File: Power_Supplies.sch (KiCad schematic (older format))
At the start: 82 parts, among them J1 Conn_HDR_2x10_latching, M1 2N7002BK, M2 2N7002BK, Q11 2N7002BK, Q12 2N7002BK, Q13 2N7002BK, Q14 2N7002BK, Q6 2N7002BK, Q7 2N7002BK, Q8 2N7002BK, Q9 2N7002BK, U22 BD50FC0WEFJ-E2, U23 LDL212D33R

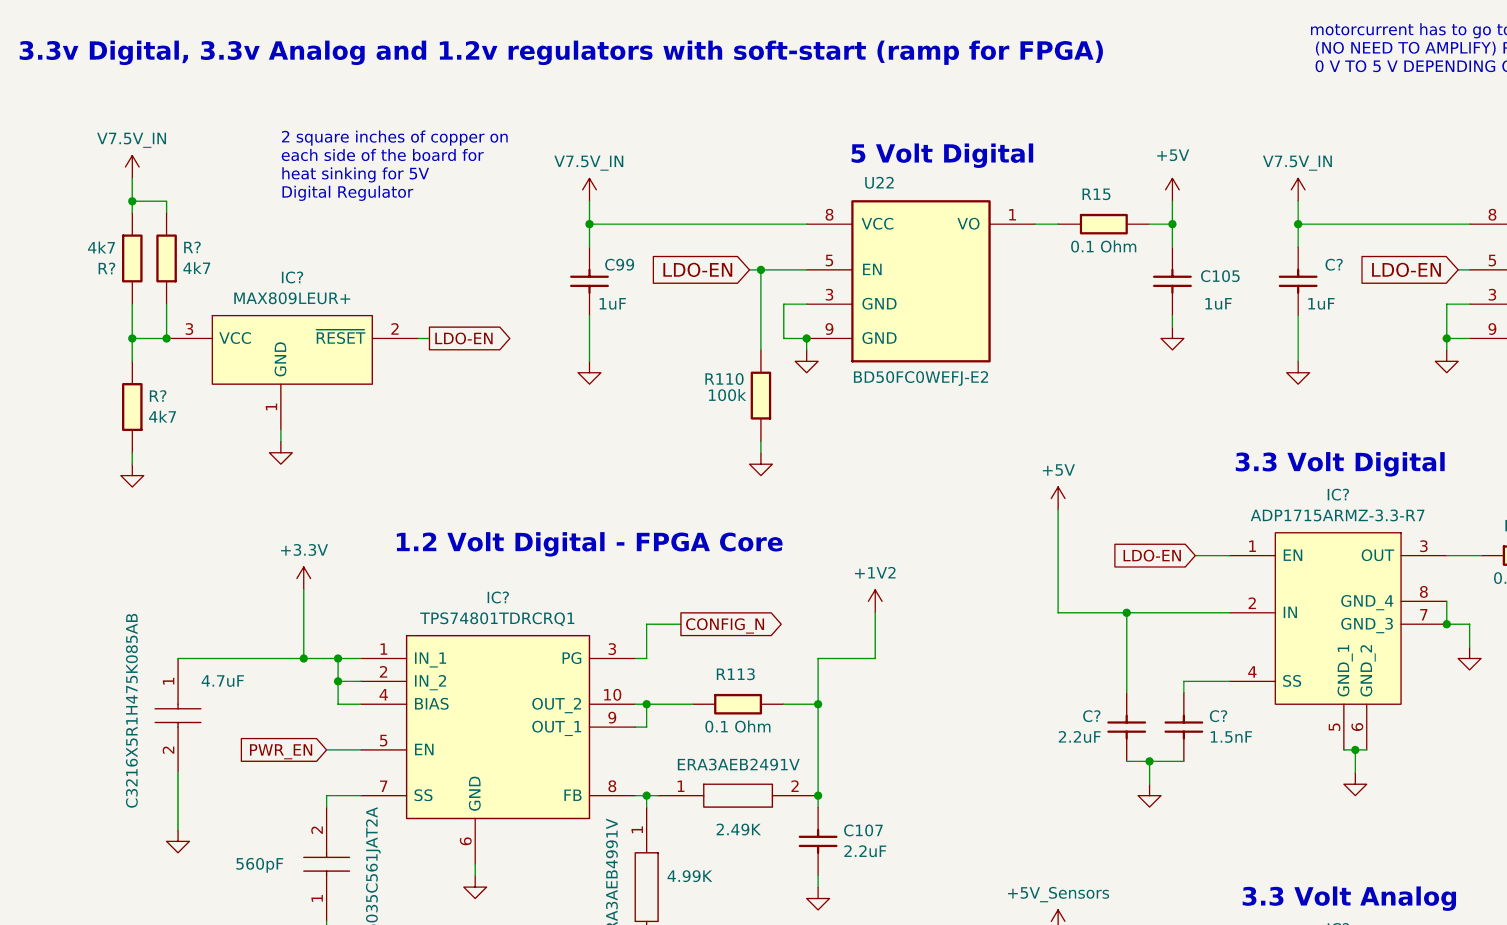
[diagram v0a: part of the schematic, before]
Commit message: Update Power_Supplies.sch
changed 7.5v_in for regulators to v7.5 after filter..
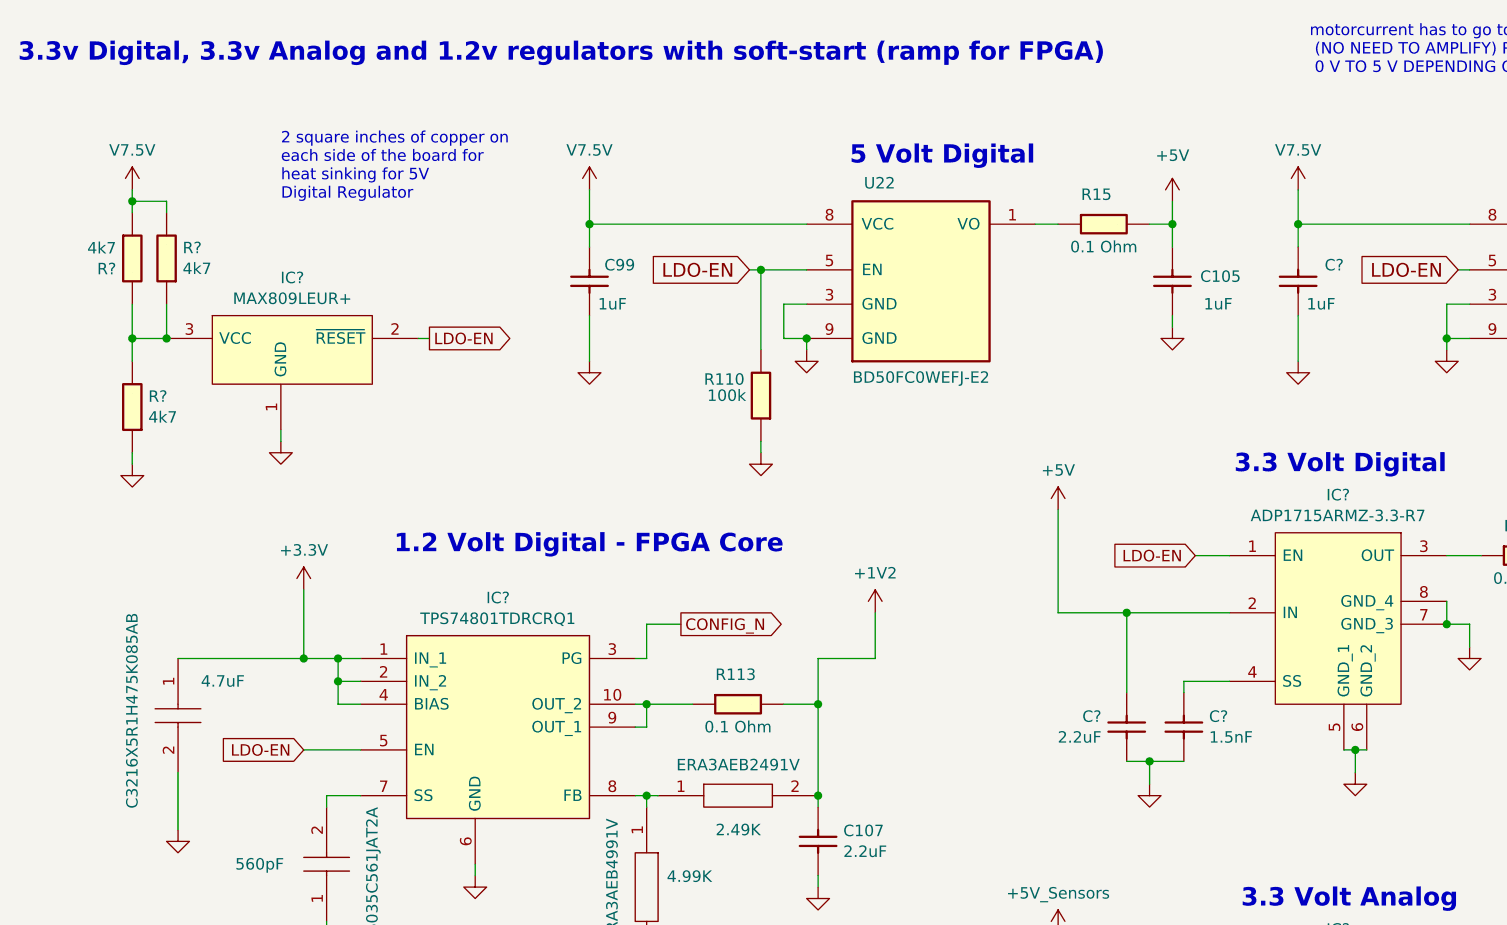
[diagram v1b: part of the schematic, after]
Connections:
- net PWR_EN is gone; now on net LDO-EN: IC?.5 (EN)
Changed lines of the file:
@@
 	1    0    0    -1
 $EndComp
-Text GLabel 1550 3250 0    50   Input ~ 0
-PWR_EN
 Wire Wire Line
 	3550 3050 3700 3050
@@
 	4850 7200 5000 7200
 Connection ~ 5300 6450
-$Comp
-L OpenVent:V7.5V_IN #PWR0162
-U 1 1 60A27BFC
-P 700 750
-F 0 "#PWR0162" H 700 600 50  0001 C CNN
-F 1 "V7.5V_IN" H 700 923 50  0000 C CNN
-F 2 "" H 700 750 50  0001 C CNN
-F 3 "" H 700 750 50  0001 C CNN
-	1    700  750
-	1    0    0    -1
-$EndComp
 Wire Wire Line
 	850  4550 850  4600
@@
 Wire Wire Line
 	700  850  850  850
-Wire Wire Line
-	700  750  700  850
-Connection ~ 700  850
 Wire Wire Line
 	6550 1450 6450 1450
@@
 	6450 1500 6450 1450
 Connection ~ 6450 1450
-Connection ~ 5800 950
 $Comp
 L OpenVent:+5V_Sensors #PWR?
@@
 	3650 1500 3650 1450
 Connection ~ 3650 1450
-$Comp
-L OpenVent:V7.5V_IN #PWR?
-U 1 1 60E0217D
-P 5800 850
-F 0 "#PWR?" H 5800 700 50  0001 C CNN
-F 1 "V7.5V_IN" H 5800 1023 50  0000 C CNN
-F 2 "" H 5800 850 50  0001 C CNN
-F 3 "" H 5800 850 50  0001 C CNN
-	1    5800 850
-	1    0    0    -1
-$EndComp
-Wire Wire Line
-	5800 850  5800 950
-$Comp
-L OpenVent:V7.5V_IN #PWR?
-U 1 1 60E1DD65
-P 2700 850
-F 0 "#PWR?" H 2700 700 50  0001 C CNN
-F 1 "V7.5V_IN" H 2700 1023 50  0000 C CNN
-F 2 "" H 2700 850 50  0001 C CNN
-F 3 "" H 2700 850 50  0001 C CNN
-	1    2700 850
-	1    0    0    -1
-$EndComp
-Wire Wire Line
-	2700 850  2700 950
-Connection ~ 2700 950
 $Comp
 L OpenVent:+3.3V #PWR?
@@
 Connection ~ 8000 950
 Wire Wire Line
-	1700 3250 1550 3250
-Wire Wire Line
 	4750 4050 4750 4550
 Wire Wire Line
@@
 	1    0    0    -1
 $EndComp
+Text GLabel 1450 3250 0    50   Input ~ 0
+LDO-EN
+Wire Wire Line
+	1450 3250 1700 3250
+$Comp
+L OpenVent:V7.5V #PWR?
+U 1 1 60A299E8
+P 5800 800
+F 0 "#PWR?" H 5800 650 50  0001 C CNN
+F 1 "V7.5V" H 5800 973 50  0000 C CNN
+F 2 "" H 5800 800 50  0001 C CNN
+F 3 "" H 5800 800 50  0001 C CNN
+	1    5800 800
+	1    0    0    -1
+$EndComp
+$Comp
+L OpenVent:V7.5V #PWR?
+U 1 1 60A29F0E
+P 2700 800
+F 0 "#PWR?" H 2700 650 50  0001 C CNN
+F 1 "V7.5V" H 2700 973 50  0000 C CNN
+F 2 "" H 2700 800 50  0001 C CNN
+F 3 "" H 2700 800 50  0001 C CNN
+	1    2700 800
+	1    0    0    -1
+$EndComp
+Wire Wire Line
+	5800 800  5800 950
+Connection ~ 5800 950
+Wire Wire Line
+	2700 800  2700 950
+Connection ~ 2700 950
+$Comp
+L OpenVent:V7.5V #PWR?
+U 1 1 60A947BC
+P 700 800
+F 0 "#PWR?" H 700 650 50  0001 C CNN
+F 1 "V7.5V" H 700 973 50  0000 C CNN
+F 2 "" H 700 800 50  0001 C CNN
+F 3 "" H 700 800 50  0001 C CNN
+	1    700  800
+	1    0    0    -1
+$EndComp
+Wire Wire Line
+	700  800  700  850
+Connection ~ 700  850
 $EndSCHEMATC

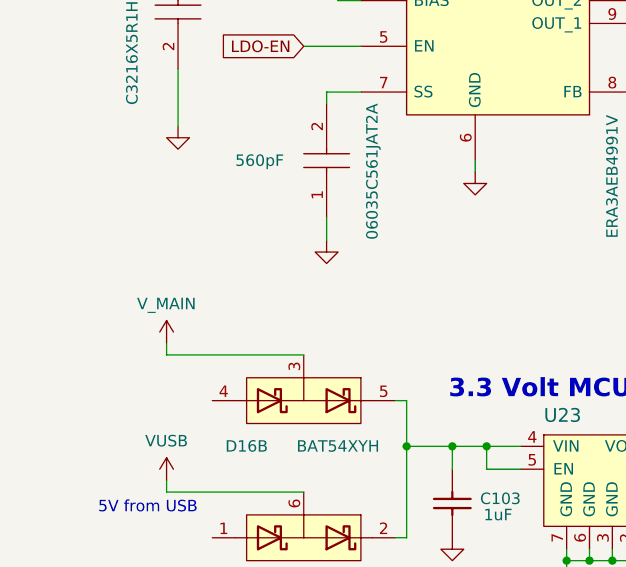
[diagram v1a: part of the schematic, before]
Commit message: Update Power_Supplies.sch
7.5V input signals corrected for regulator
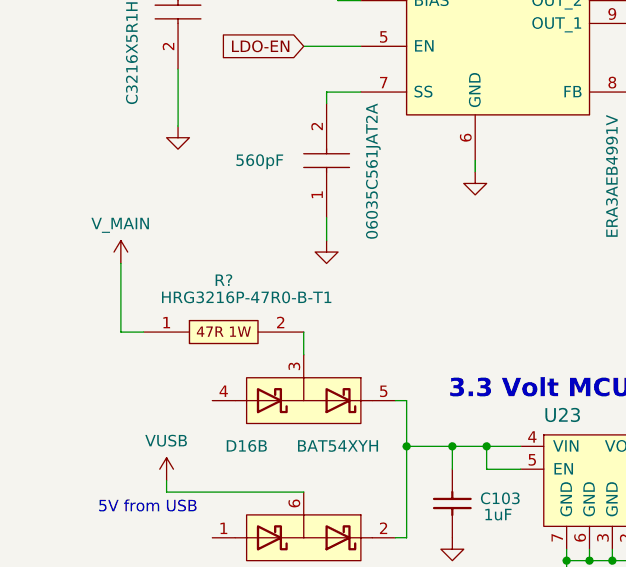
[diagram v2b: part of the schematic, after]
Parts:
- added R?: HRG3216P-47R0-B-T1, RESC3216X55N, symbol OpenVent:HRG3216P-47R0-B-T1
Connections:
- net V_MAIN: now also R?.1; no longer D16.3 (A3;K4)
- new net: D16.3 (A3;K4), R?.2
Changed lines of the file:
@@
 	850  5200 1450 5200
-Wire Wire Line
-	1450 4600 850  4600
 Wire Wire Line
 	2950 6700 2950 6550
@@
 	4850 7200 5000 7200
 Connection ~ 5300 6450
-Wire Wire Line
-	850  4550 850  4600
 Text Notes 6400 6700 2    50   ~ 0
 Power UP LED
@@
 L OpenVent:V_MAIN #PWR0160
 U 1 1 60C8A7AC
-P 850 4550
-F 0 "#PWR0160" H 850 4400 50  0001 C CNN
-F 1 "V_MAIN" H 850 4723 50  0000 C CNN
-F 2 "" H 850 4550 50  0001 C CNN
-F 3 "" H 850 4550 50  0001 C CNN
-	1    850  4550
+P 650 4200
+F 0 "#PWR0160" H 650 4050 50  0001 C CNN
+F 1 "V_MAIN" H 650 4373 50  0000 C CNN
+F 2 "" H 650 4200 50  0001 C CNN
+F 3 "" H 650 4200 50  0001 C CNN
+	1    650  4200
 	1    0    0    -1
 $EndComp
@@
 	700  800  700  850
 Connection ~ 700  850
+$Comp
+L OpenVent:HRG3216P-47R0-B-T1 R?
+U 1 1 60A949A4
+P 750 4500
+F 0 "R?" H 1100 4725 50  0000 C CNN
+F 1 "HRG3216P-47R0-B-T1" H 1200 4650 50  0000 C CNN
+F 2 "RESC3216X55N" H 1300 4550 50  0001 L CNN
+F 3 "http://www.susumu.co.jp/common/pdf/n_catalog_partition24_en.pdf" H 1300 4450 50  0001 L CNN
+F 4 "RES SMD 47 OHM 0.1% 1W 1206" H 1300 4350 50  0001 L CNN "Description"
+F 5 "0.55" H 1300 4250 50  0001 L CNN "Height"
+F 6 "Susumu" H 1300 4150 50  0001 L CNN "Manufacturer_Name"
+F 7 "HRG3216P-47R0-B-T1" H 1300 4050 50  0001 L CNN "Manufacturer_Part_Number"
+F 8 "754-HRG3216P47R0BT1" H 1300 3950 50  0001 L CNN "Mouser Part Number"
+F 9 "https://www.mouser.com/Search/Refine.aspx?Keyword=754-HRG3216P47R0BT1" H 1300 3850 50  0001 L CNN "Mouser Price/Stock"
+	1    750  4500
+	1    0    0    -1
+$EndComp
+Wire Wire Line
+	1450 4500 1450 4600
+Wire Wire Line
+	750  4500 650  4500
+Wire Wire Line
+	650  4200 650  4500
 $EndSCHEMATC

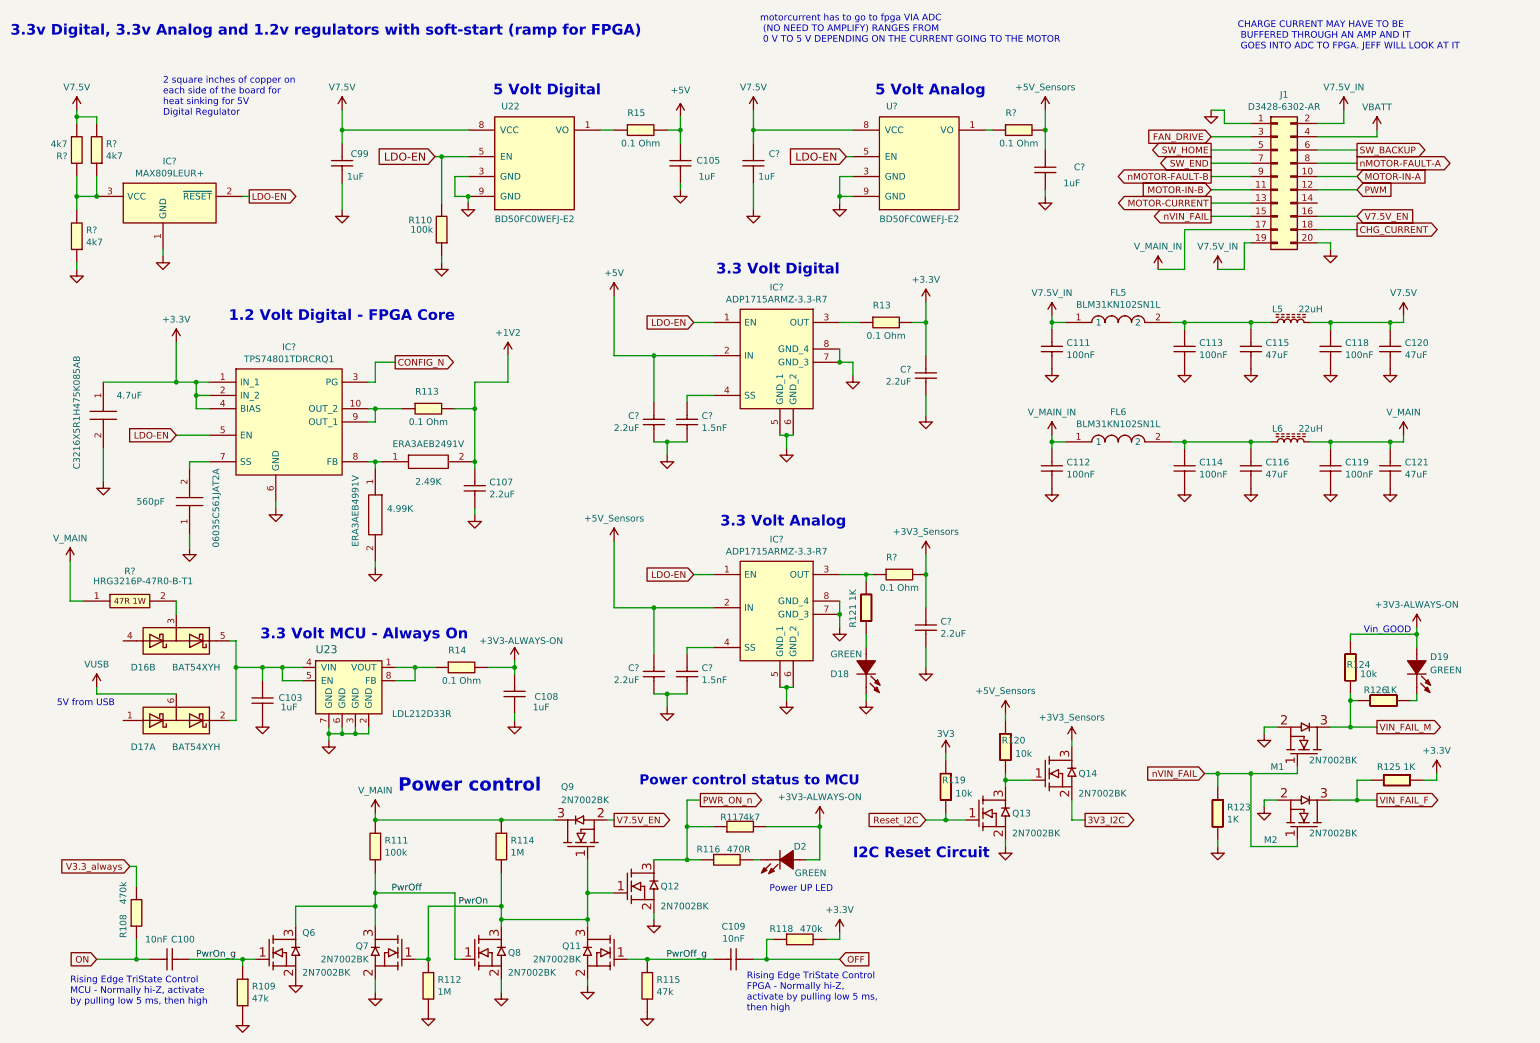
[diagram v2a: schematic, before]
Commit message: Beginning the process of design review, fixed a couple howlers.
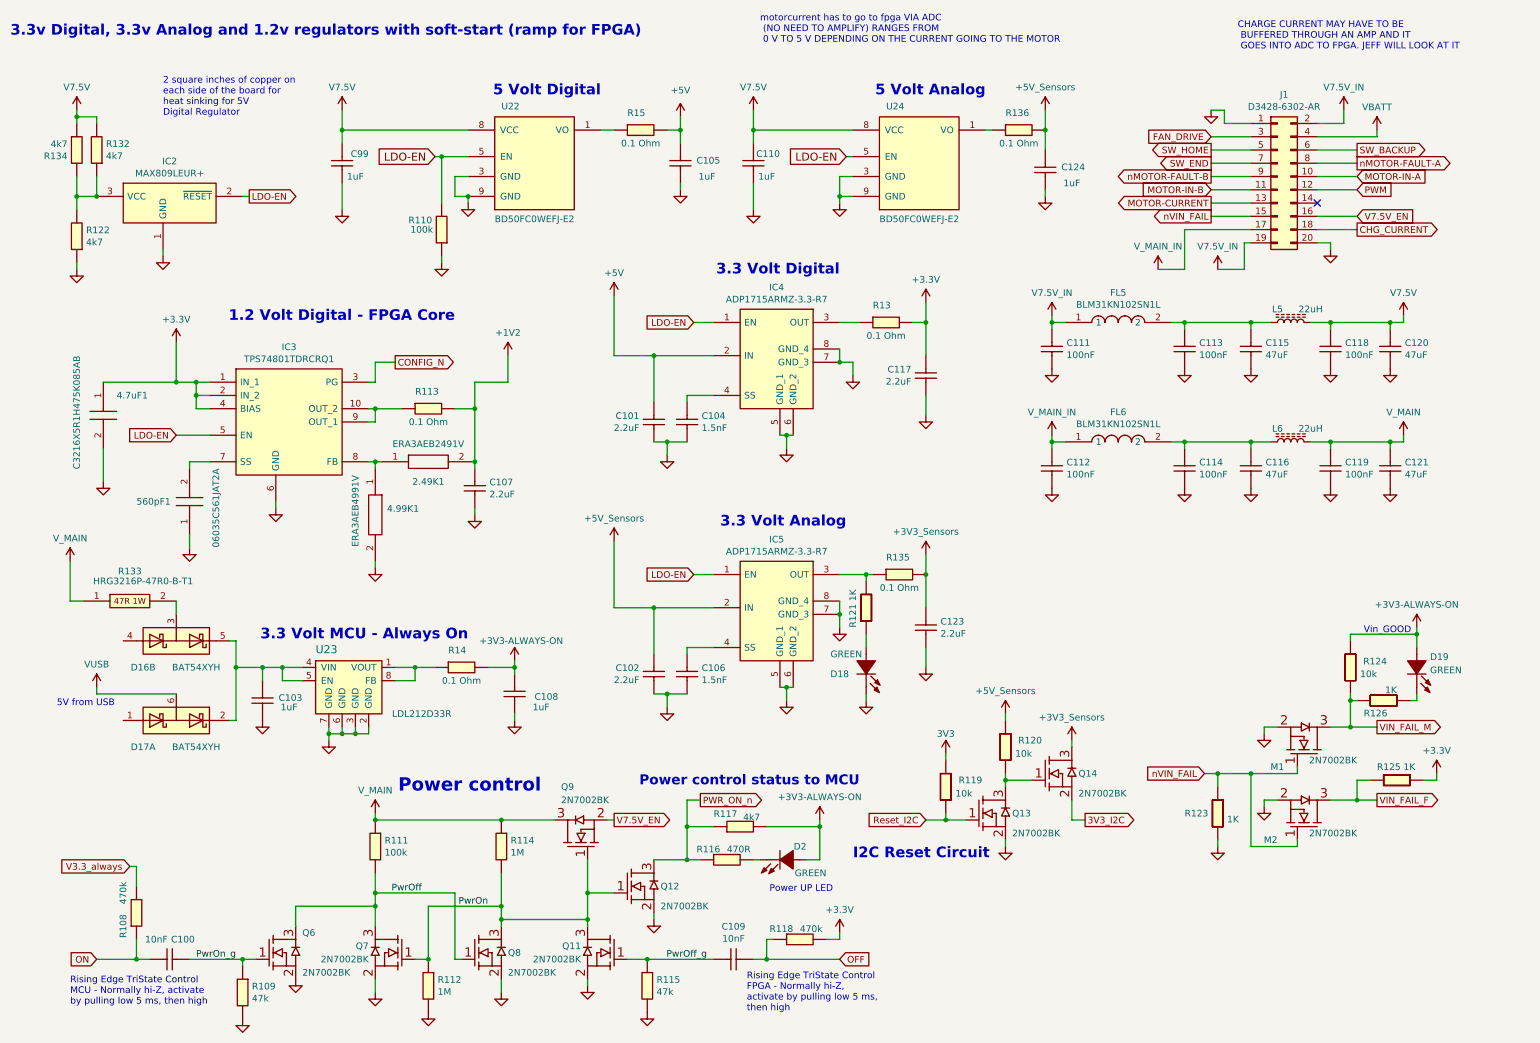
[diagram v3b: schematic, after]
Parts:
- gave numbers to parts that had none: 19
- renumbered 2.49K to 2.49K1, 4.7uF to 4.7uF1, 4.99K to 4.99K1, 560pF to 560pF1
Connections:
- no-connect marks 0 -> 1

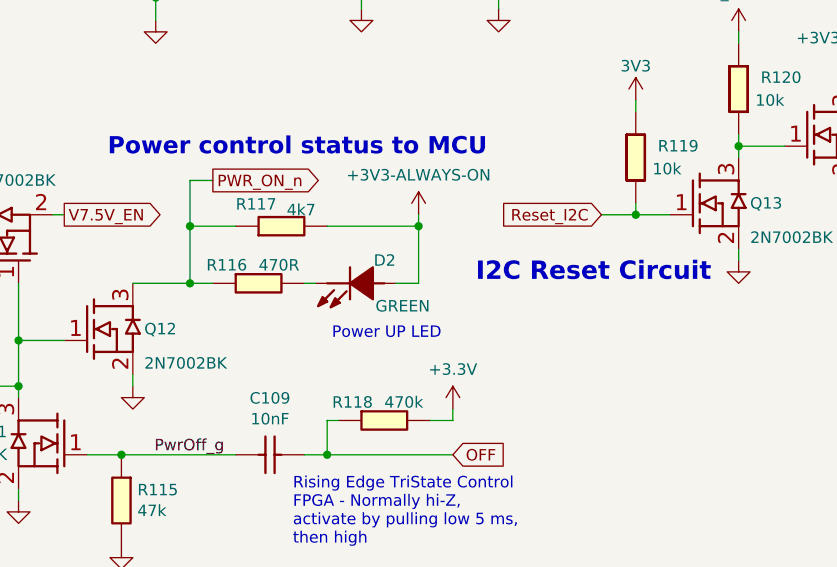
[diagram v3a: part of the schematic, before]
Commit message: add footprint
new footprint was added to parts without footprint
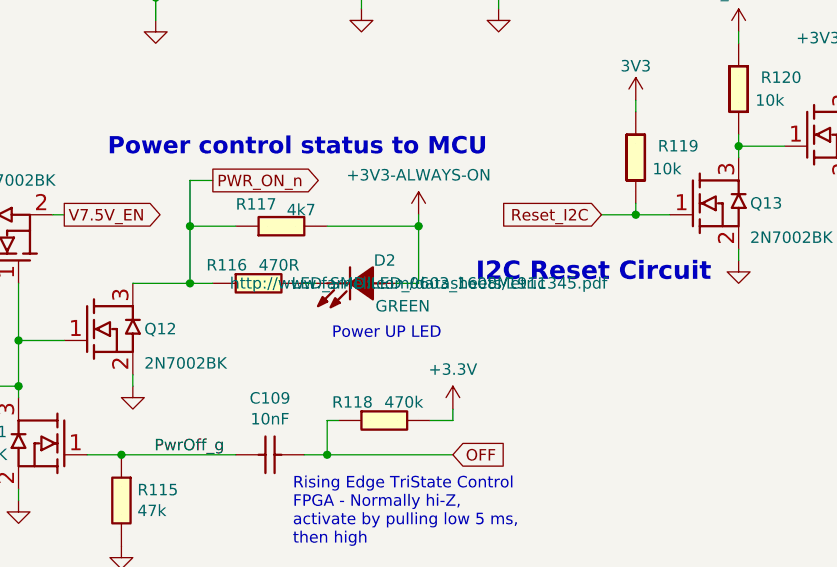
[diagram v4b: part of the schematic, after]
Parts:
- D2: footprint (none) -> LED_SMD:LED_0603_1608Metric
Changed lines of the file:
@@
 F 0 "D2" H 6400 6350 50  0000 L CNN
 F 1 "LED_GREEN_0603_SMD" H 6300 6450 60  0001 C CNN
-F 2 "" H 6300 6450 50  0000 C CNN
-F 3 "" H 6300 6450 50  0000 C CNN
+F 2 "LED_SMD:LED_0603_1608Metric" H 6300 6450 50  0000 C CNN
+F 3 "http://www.farnell.com/datasheets/1911345.pdf" H 6300 6450 50  0000 C CNN
 F 4 "GREEN" H 6250 6550 50  0000 L CNN "Val"
 	1    6300 6450
